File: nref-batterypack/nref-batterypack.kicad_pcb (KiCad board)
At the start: 4 copper layers, 75 x 17 mm, 66 parts, among them J1 BACK_CONN, J2 C4+, J3 C3-, J4 C2+, J5 C1-, J6 C1-, J7 PACK_CONN, Q1 BC817, Q2 BC817, Q3 BC817, Q4 BC817, Q5 AO3401A, Q6 DMT2005UDV, Q7 AO3401A, SW1 Reset, U1 BQ76922

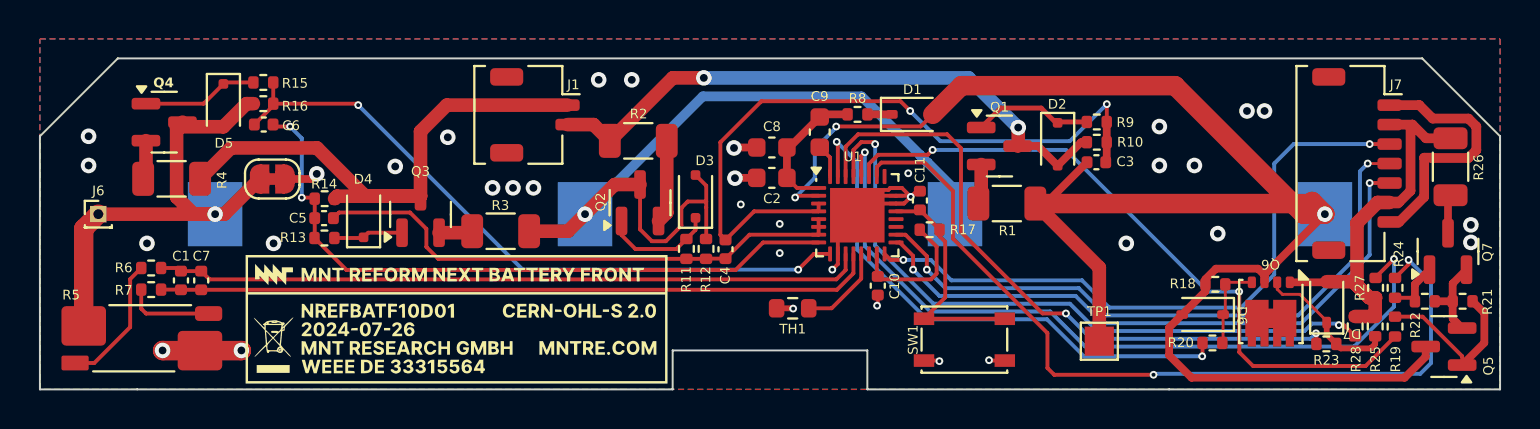
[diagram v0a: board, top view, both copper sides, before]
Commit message: batterypack front/back: update board outline/mounting holes
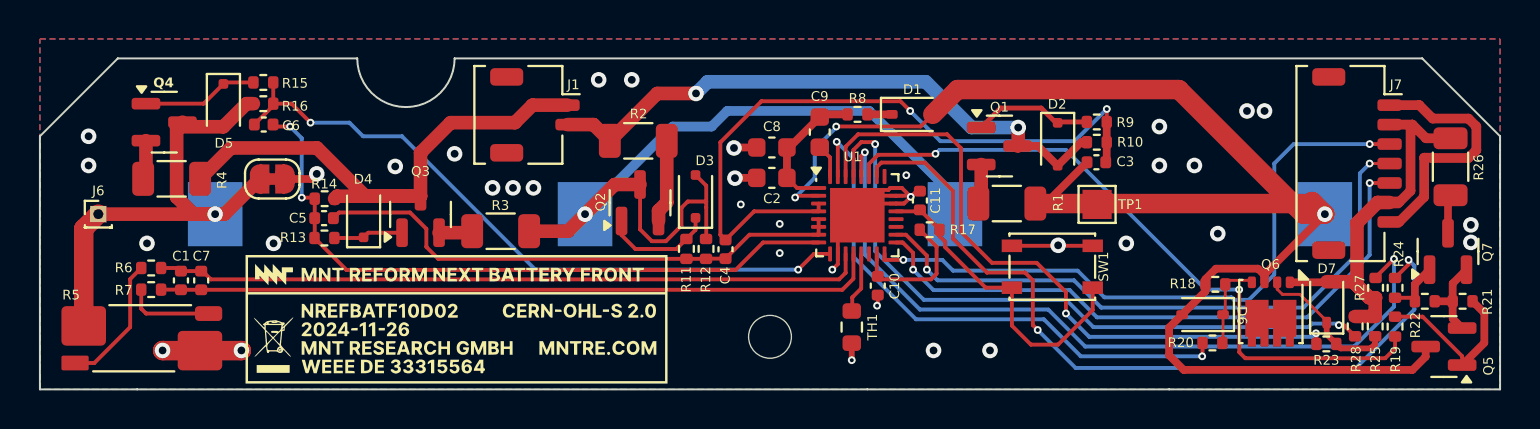
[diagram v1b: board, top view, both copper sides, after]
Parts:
- added H1: MountingHole, MountingHole:MountingHole_2.2mm_M2, F.Cu at (137.5, 105.3)
- moved TP1 7.03 mm to (154.3, 98.5)
- moved SW1 5.87 mm to (152.0, 101.7), turned to 0 degrees
- moved TH1 3.18 mm to (141.7, 104.8), turned to -90 degrees
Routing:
- net /BAT+: track 89.6 -> 83.9 mm
- net /~{RST}: track 12.0 -> 16.4 mm
- net /PDSG: track 43.3 -> 40.5 mm
- net GND: track 20.9 -> 23.4 mm, vias 13 -> 12
- net Net-(U1-TS1): track 4.60 -> 2.98 mm
- net Net-(D3-A): track 42.3 -> 41.5 mm
- net /C1+: track 29.0 -> 28.4 mm
- net /DSG: track 33.5 -> 34.1 mm
- net /PACK-: vias 22 -> 24
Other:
- outline, holes or cut-outs redrawn
